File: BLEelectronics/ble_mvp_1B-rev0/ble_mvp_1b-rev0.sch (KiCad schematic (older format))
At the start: 32 parts, among them IC1 LTC4412xS6, IC2 LTC4054LES5-4.2#TRPBF, IC3 PCF8523T, IC4 MX25R6435FM2IL0, J1 USB_B_Micro, Q1 Si2307CDS, U1 BAT-HLD-001, U2 ESD401, U3 ESD401, U4 LP5907MFX-3.3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

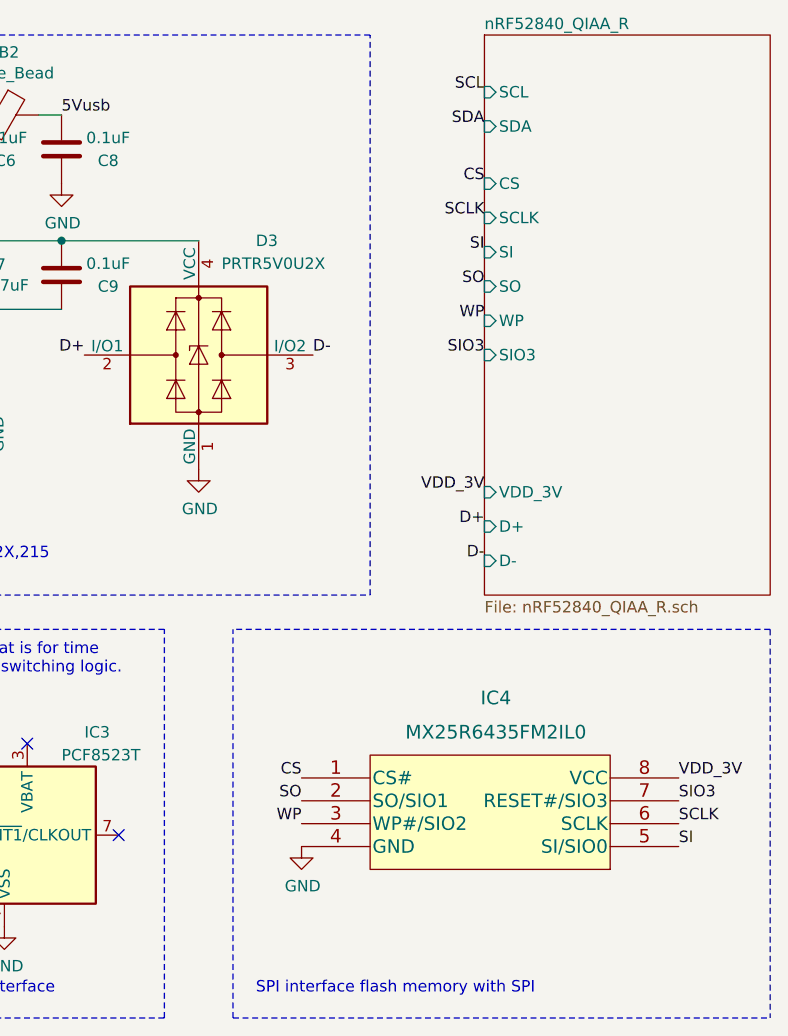
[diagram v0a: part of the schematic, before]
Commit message: correct CS to CS# in schematic and pdfs for all mvps
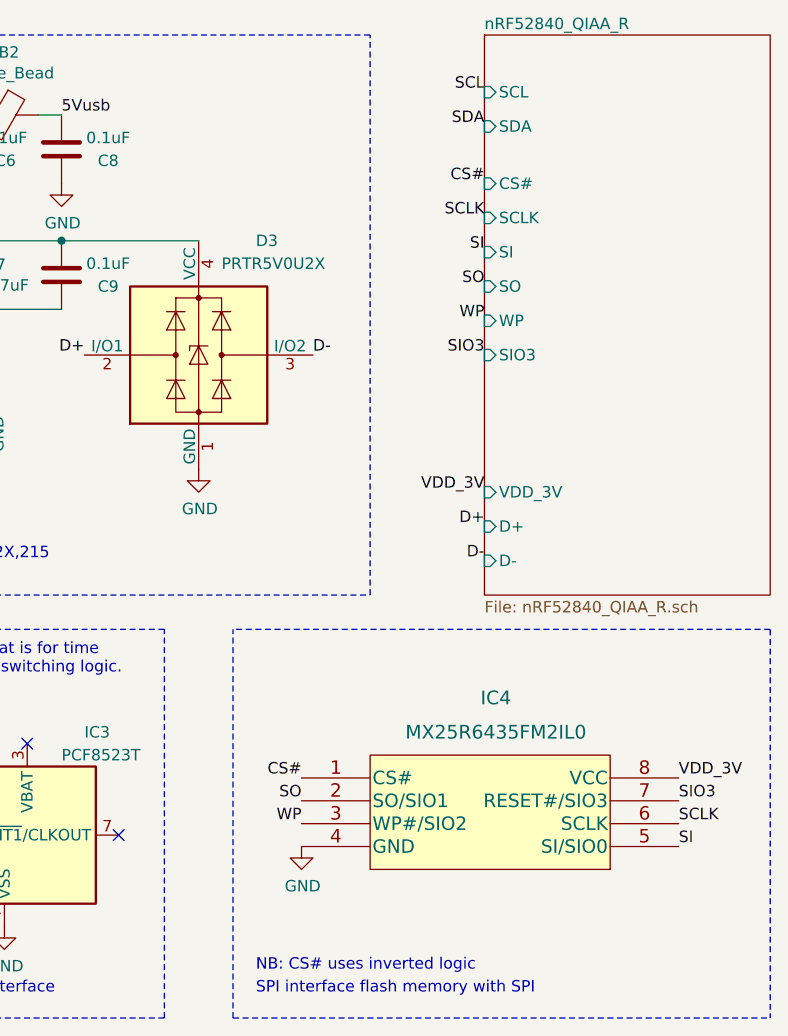
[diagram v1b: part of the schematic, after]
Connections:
- net CS renamed CS#
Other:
- note added: "NB: CS# uses inverted logic"
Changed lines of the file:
@@
 F1 "nRF52840_QIAA_R.sch" 50
 F2 "SCL" I L 9550 2400 50
-F3 "CS" I L 9550 2800 50
-F4 "SCLK" I L 9550 2950 50
-F5 "SI" I L 9550 3100 50
-F6 "SO" I L 9550 3250 50
-F7 "WP" I L 9550 3400 50
-F8 "SIO3" I L 9550 3550 50
-F9 "SDA" I L 9550 2550 50
-F10 "VDD_3V" I L 9550 4150 50
-F11 "D+" I L 9550 4300 50
-F12 "D-" I L 9550 4450 50
+F3 "SCLK" I L 9550 2950 50
+F4 "SI" I L 9550 3100 50
+F5 "SO" I L 9550 3250 50
+F6 "WP" I L 9550 3400 50
+F7 "SIO3" I L 9550 3550 50
+F8 "SDA" I L 9550 2550 50
+F9 "VDD_3V" I L 9550 4150 50
+F10 "D+" I L 9550 4300 50
+F11 "D-" I L 9550 4450 50
+F12 "CS#" I L 9550 2800 50
 $EndSheet
 $Comp
@@
 SIO3
 Text Label 8750 5400 2    50   ~ 0
-CS
+CS#
 Text Label 8750 5600 2    50   ~ 0
 WP
@@
 SO
 Text Label 9550 2800 2    50   ~ 0
-CS
+CS#
 Text Label 9550 3400 2    50   ~ 0
 WP
@@
 	1    0    0    -1
 $EndComp
+Text Notes 8550 6250 0    50   ~ 0
+NB: CS# uses inverted logic
 $EndSCHEMATC

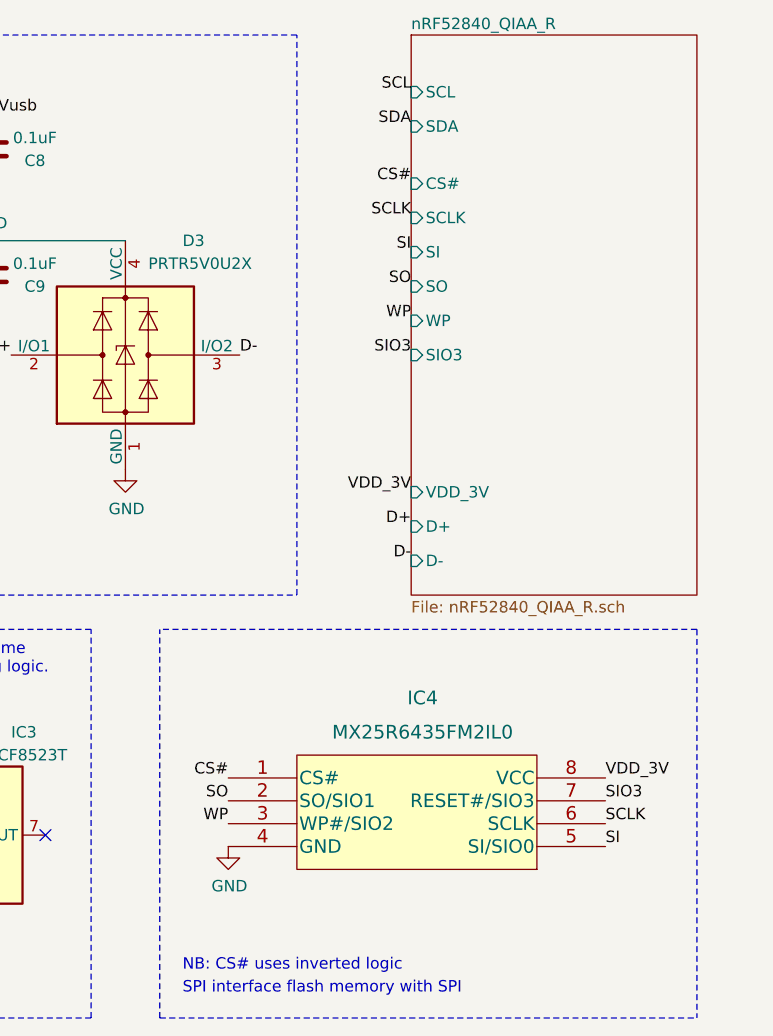
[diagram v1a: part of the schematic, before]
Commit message: Additional changes to schematic labelling.
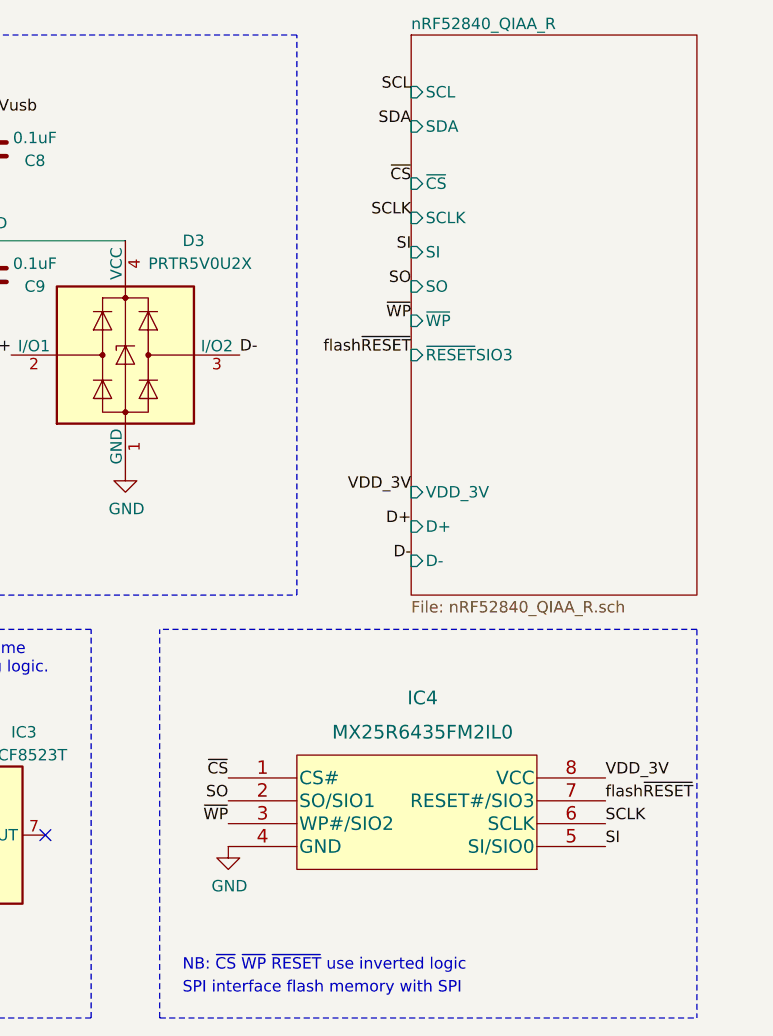
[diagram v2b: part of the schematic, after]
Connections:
- net CS# renamed ~CS~
- net SIO3 renamed flash~RESET~
- net WP renamed ~WP~
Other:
- note added: "NB: ~CS~ ~WP~ ~RESET~ use inverted logic"
- note removed: "NB: CS# uses inverted logic"
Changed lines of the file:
@@
 F4 "SI" I L 9550 3100 50
 F5 "SO" I L 9550 3250 50
-F6 "WP" I L 9550 3400 50
-F7 "SIO3" I L 9550 3550 50
-F8 "SDA" I L 9550 2550 50
-F9 "VDD_3V" I L 9550 4150 50
-F10 "D+" I L 9550 4300 50
-F11 "D-" I L 9550 4450 50
-F12 "CS#" I L 9550 2800 50
+F6 "SDA" I L 9550 2550 50
+F7 "VDD_3V" I L 9550 4150 50
+F8 "D+" I L 9550 4300 50
+F9 "D-" I L 9550 4450 50
+F10 "~CS" I L 9550 2800 50
+F11 "~WP" I L 9550 3400 50
+F12 "~RESET~SIO3" I L 9550 3550 50
 $EndSheet
 $Comp
@@
 SO
 Text Label 10400 5500 0    50   ~ 0
-SIO3
+flash~RESET~
 Text Label 8750 5400 2    50   ~ 0
-CS#
+~CS~
 Text Label 8750 5600 2    50   ~ 0
-WP
+~WP~
 Text Label 6650 5050 0    50   ~ 0
 VDD_3V
@@
 SO
 Text Label 9550 2800 2    50   ~ 0
-CS#
+~CS~
 Text Label 9550 3400 2    50   ~ 0
-WP
+~WP
 Text Label 9550 4150 2    50   ~ 0
 VDD_3V
@@
 3V
 Text Label 9550 3550 2    50   ~ 0
-SIO3
+flash~RESET~
 Text Notes 6200 1050 0    50   ~ 0
 Q: Do we change the ESD to be the same as the dongle? PRTR5V0U2X
@@
 $EndComp
 Text Notes 8550 6250 0    50   ~ 0
-NB: CS# uses inverted logic
+NB: ~CS~ ~WP~ ~RESET~ use inverted logic
 $EndSCHEMATC

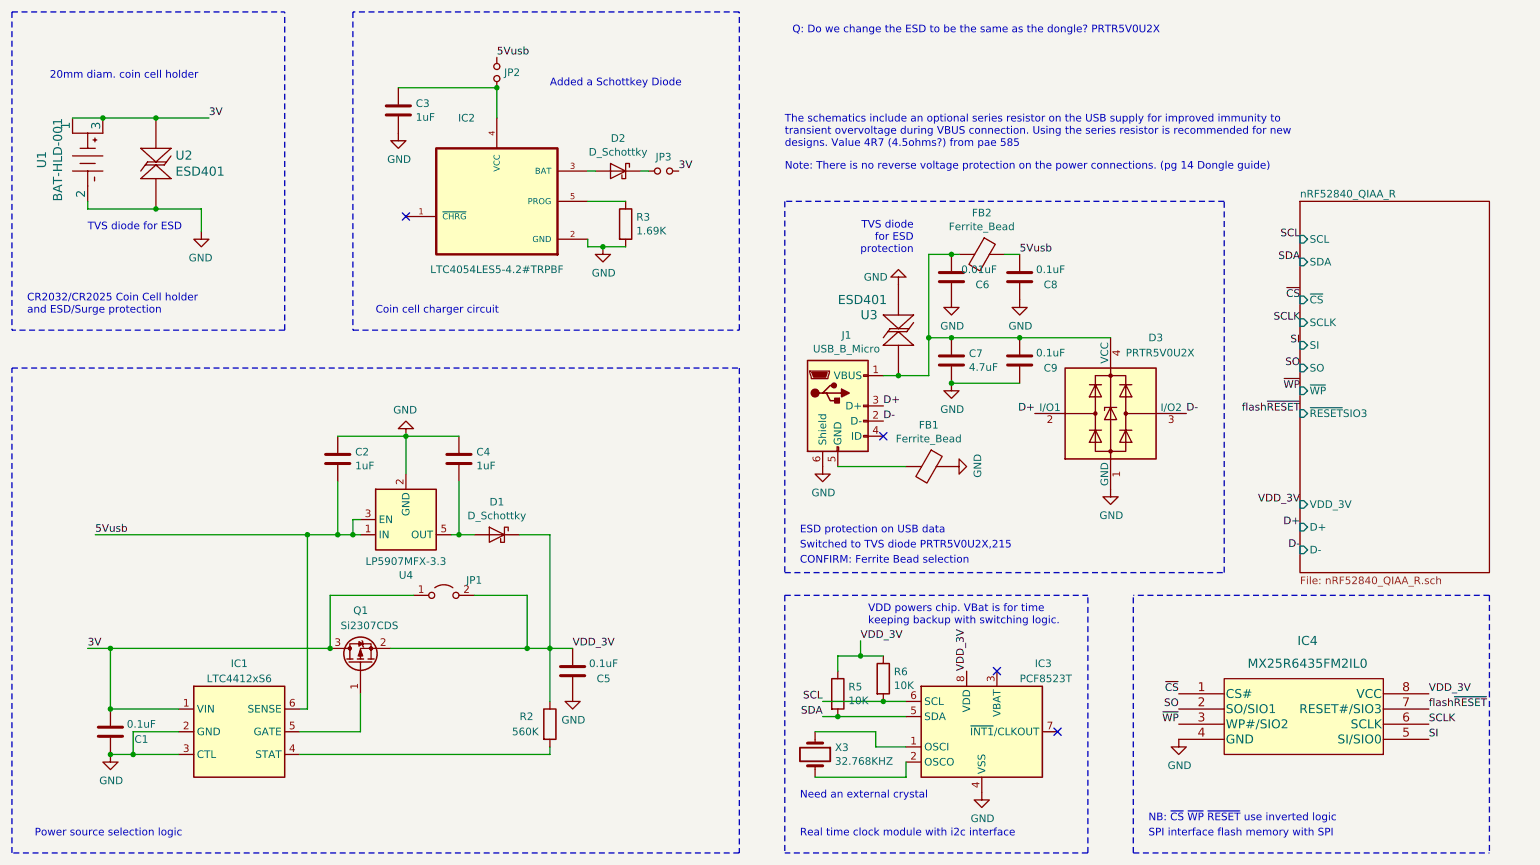
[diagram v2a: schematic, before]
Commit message: increased track widths on long traces on mvp1b-rev0
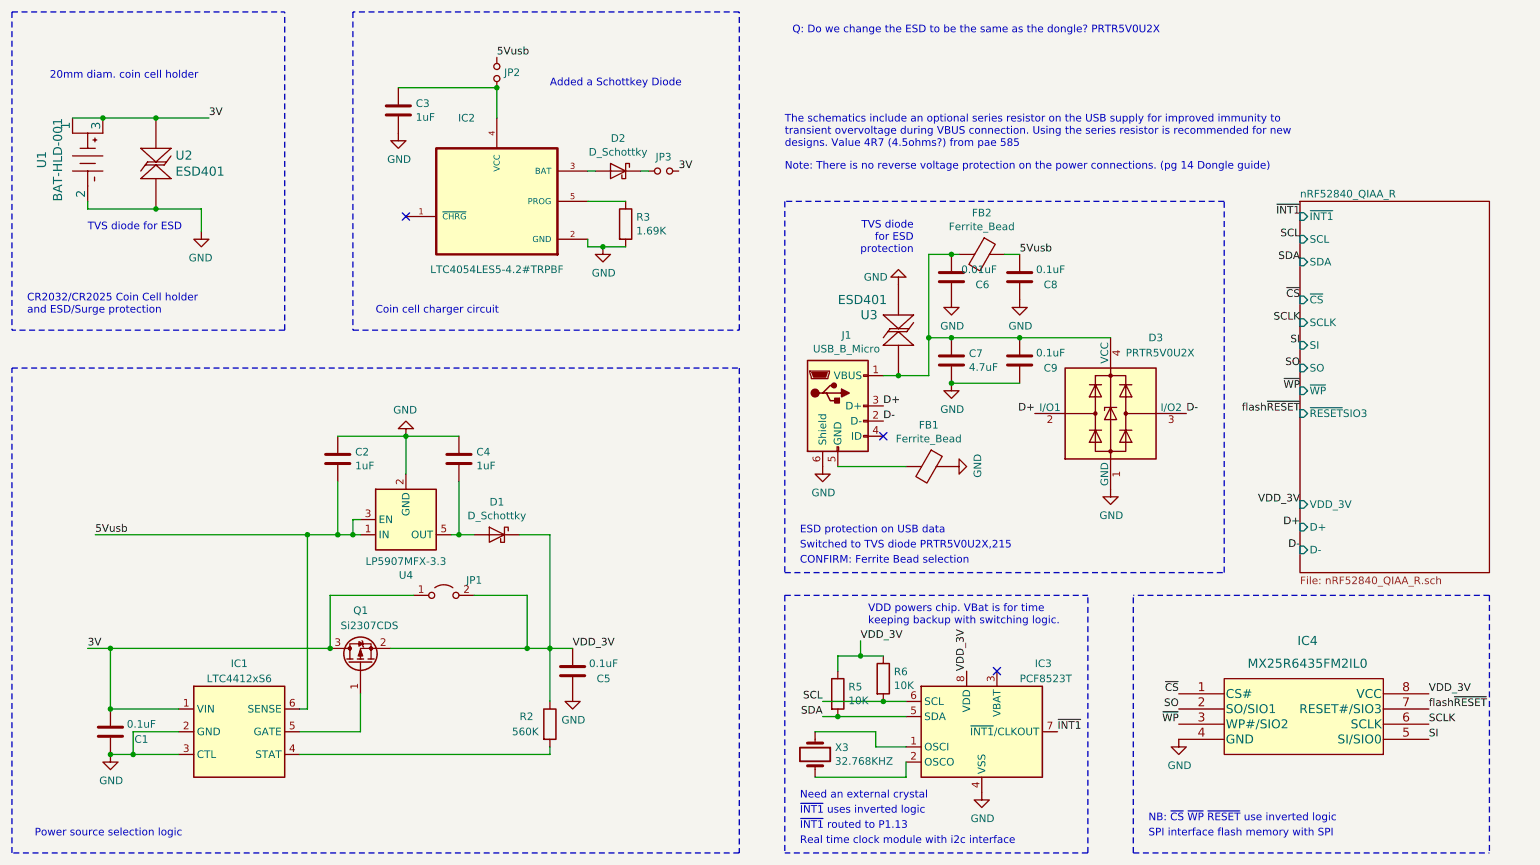
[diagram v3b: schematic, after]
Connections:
- net ~INT1~: now reaches IC3.7 (~INT1~/CLKOUT)
- no-connect marks 4 -> 3
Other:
- note added: "~INT1~ routed to P1.13"
- note added: "~INT1~ uses inverted logic"
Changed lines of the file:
@@
 F11 "~WP" I L 9550 3400 50
 F12 "~RESET~SIO3" I L 9550 3550 50
+F13 "~INT1~" I L 9550 2250 50
 $EndSheet
 $Comp
@@
 Text Label 7350 5250 1    50   ~ 0
 VDD_3V
-Text Notes 6250 6350 0    50   ~ 0
+Text Notes 6250 6400 0    50   ~ 0
 Real time clock module with i2c interface
 Text Label 6400 5450 2    50   ~ 0
@@
 NoConn ~ 3650 2250
 NoConn ~ 6800 3700
-NoConn ~ 7950 5650
 NoConn ~ 7550 5250
 $Comp
@@
 Text Notes 8550 6250 0    50   ~ 0
 NB: ~CS~ ~WP~ ~RESET~ use inverted logic
+Text Label 7950 5650 0    50   ~ 0
+~INT1~
+Text Label 9550 2250 2    50   ~ 0
+~INT1~
+Text Notes 6250 6200 0    50   ~ 0
+~INT1~ uses inverted logic
+Text Notes 6250 6300 0    50   ~ 0
+~INT1~ routed to P1.13
 $EndSCHEMATC
